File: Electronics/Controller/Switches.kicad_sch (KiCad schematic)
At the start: 5 parts, among them J20 SWITCHES

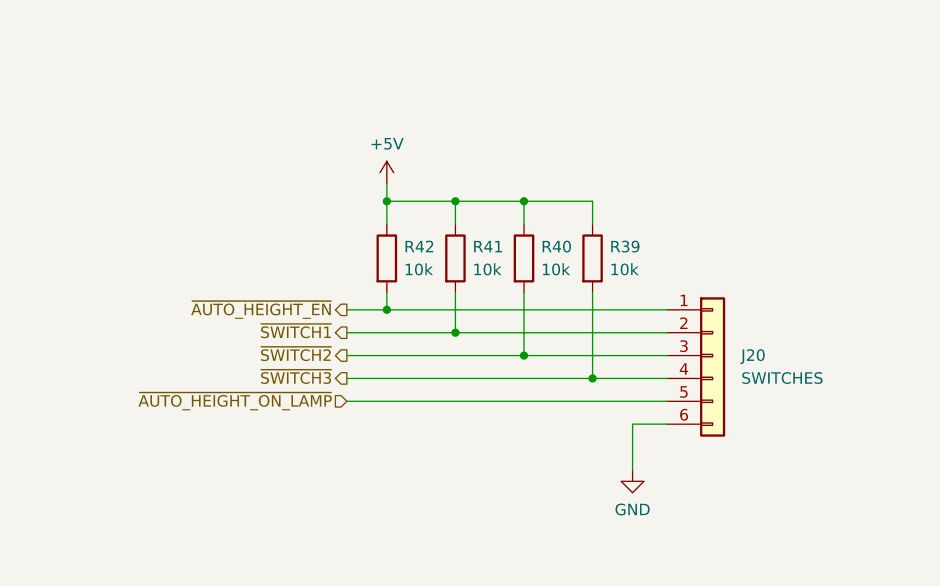
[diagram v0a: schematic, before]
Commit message: Updated schematic. Added footprints for all components.
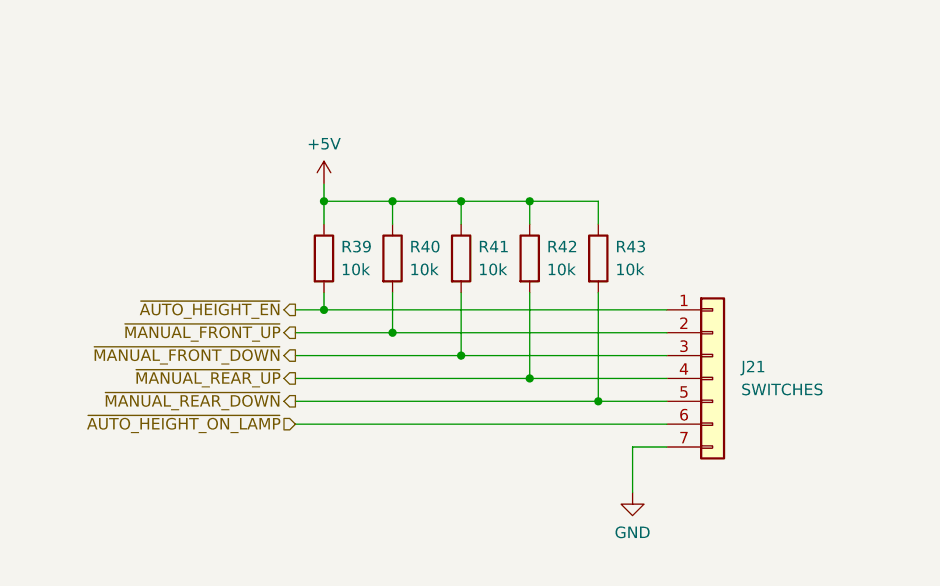
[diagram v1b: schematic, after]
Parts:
- added R43: 10k, Resistor_SMD:R_0805_2012Metric, symbol Device:R
- J21: renamed from J20; footprint (none) -> Connector_JST:JST_PH_B7B-PH-K_1x07_P2.00mm_Vertical; symbol Connector_Generic:Conn_01x06 -> Connector_Generic:Conn_01x07; manf# (none) -> B7B-PH-K-S
- R39: renamed from R42; footprint (none) -> Resistor_SMD:R_0805_2012Metric
- R40: renamed from R41; footprint (none) -> Resistor_SMD:R_0805_2012Metric
- R41: renamed from R40; footprint (none) -> Resistor_SMD:R_0805_2012Metric
- R42: renamed from R39; footprint (none) -> Resistor_SMD:R_0805_2012Metric
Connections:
- net +5V: now also R43.1
- net GND: now also J21.7 (Pin_7); no longer J21.6 (Pin_6)
- net ~{AUTO_HEIGHT_ON_LAMP}: now also J21.6 (Pin_6); no longer J21.5 (Pin_5)
- net ~{SWITCH1} renamed ~{MANUAL_FRONT_UP}
- net ~{SWITCH2} renamed ~{MANUAL_FRONT_DOWN}
- net ~{SWITCH3} renamed ~{MANUAL_REAR_UP}
- new net ~{MANUAL_REAR_DOWN}: J21.5 (Pin_5), R43.2
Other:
- moved on the sheet: R39, R40, R41, R42

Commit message: Changed switches and lamps. Removed status LEDs. Working on PCB layout.
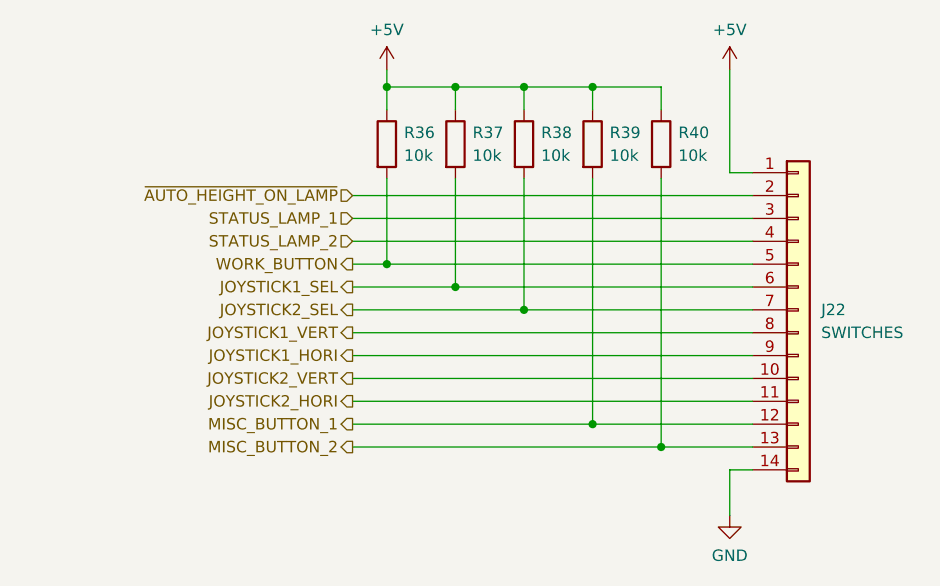
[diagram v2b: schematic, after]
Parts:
- removed R41: 10k, Resistor_SMD:R_0805_2012Metric, symbol Device:R
- added R39: 10k, Resistor_SMD:R_0805_2012Metric, symbol Device:R
- J22: renamed from J21; footprint Connector_JST:JST_PH_B7B-PH-K_1x07_P2.00mm_Vertical -> Connector_JST:JST_PH_B14B-PH-K_1x14_P2.00mm_Vertical; symbol Connector_Generic:Conn_01x07 -> Connector_Generic:Conn_01x14; manf# B7B-PH-K-S -> B14B-PH-K-S
- renumbered R39 to R36, R42 to R37, R43 to R38
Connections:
- net +5V: now also J22.1 (Pin_1), R39.1
- net GND: now also J22.14 (Pin_14); no longer J22.7 (Pin_7)
- net ~{AUTO_HEIGHT_ON_LAMP}: now also J22.2 (Pin_2); no longer J22.6 (Pin_6)
- net ~{AUTO_HEIGHT_EN} renamed WORK_BUTTON
- net WORK_BUTTON: now also J22.5 (Pin_5); no longer J22.1 (Pin_1)
- net ~{MANUAL_FRONT_DOWN} renamed STATUS_LAMP_1
- net ~{MANUAL_FRONT_UP} renamed MISC_BUTTON_2
- net MISC_BUTTON_2: now also J22.13 (Pin_13); no longer J22.2 (Pin_2)
- net ~{MANUAL_REAR_DOWN} renamed JOYSTICK2_SEL
- net JOYSTICK2_SEL: now also J22.7 (Pin_7); no longer J22.5 (Pin_5)
- net ~{MANUAL_REAR_UP} renamed JOYSTICK1_SEL
- net JOYSTICK1_SEL: now also J22.6 (Pin_6); no longer J22.4 (Pin_4)
- new net JOYSTICK1_HORI: J22.9 (Pin_9)
- new net JOYSTICK1_VERT: J22.8 (Pin_8)
- new net JOYSTICK2_HORI: J22.11 (Pin_11)
- new net JOYSTICK2_VERT: J22.10 (Pin_10)
- new net MISC_BUTTON_1: J22.12 (Pin_12), R39.2
- new net STATUS_LAMP_2: J22.4 (Pin_4)
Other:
- moved on the sheet: R36, R37, R38
